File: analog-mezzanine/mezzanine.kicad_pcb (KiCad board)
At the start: 2 copper layers, 90 x 90 mm, 133 parts, among them J7 LD15P24A4GV00LF, U1 minus TPS7A3001MDGNTEP, U10 minus TPS7A3001MDGNTEP, U11 plus TPS7A4901DGNT, U12 BUF602xDBV, U2 plus TPS7A4901DGNT, U3 BUF602xDBV, U4 minus TPS7A3001MDGNTEP, U5 plus TPS7A4901DGNT, U6 BUF602xDBV, U7 minus TPS7A3001MDGNTEP, U8 plus TPS7A4901DGNT, U9 BUF602xDBV

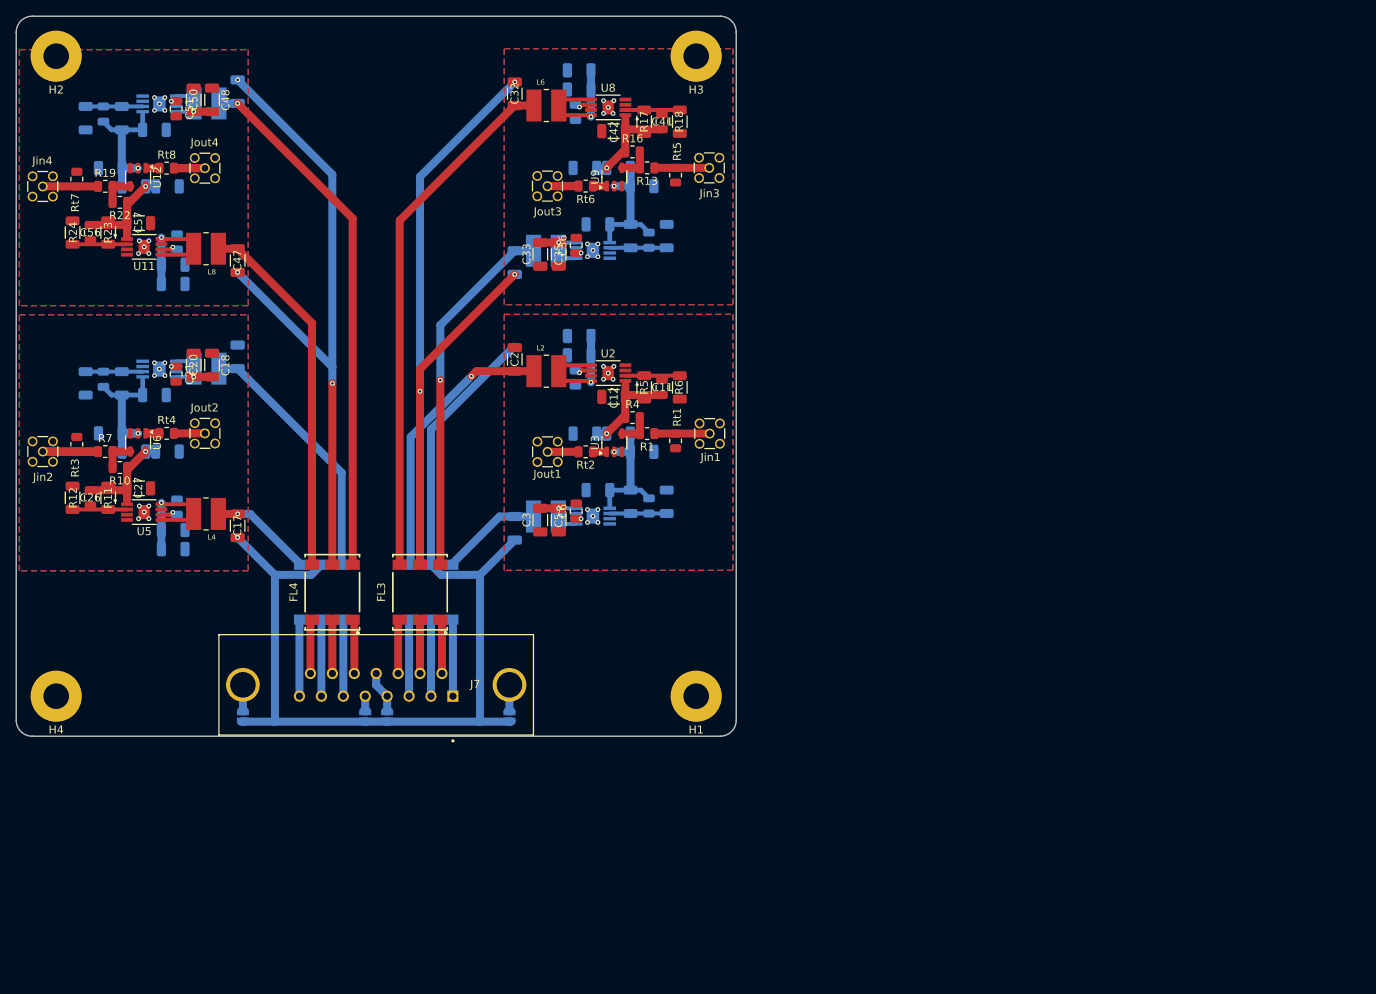
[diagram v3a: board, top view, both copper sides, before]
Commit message: update layout: central D connector
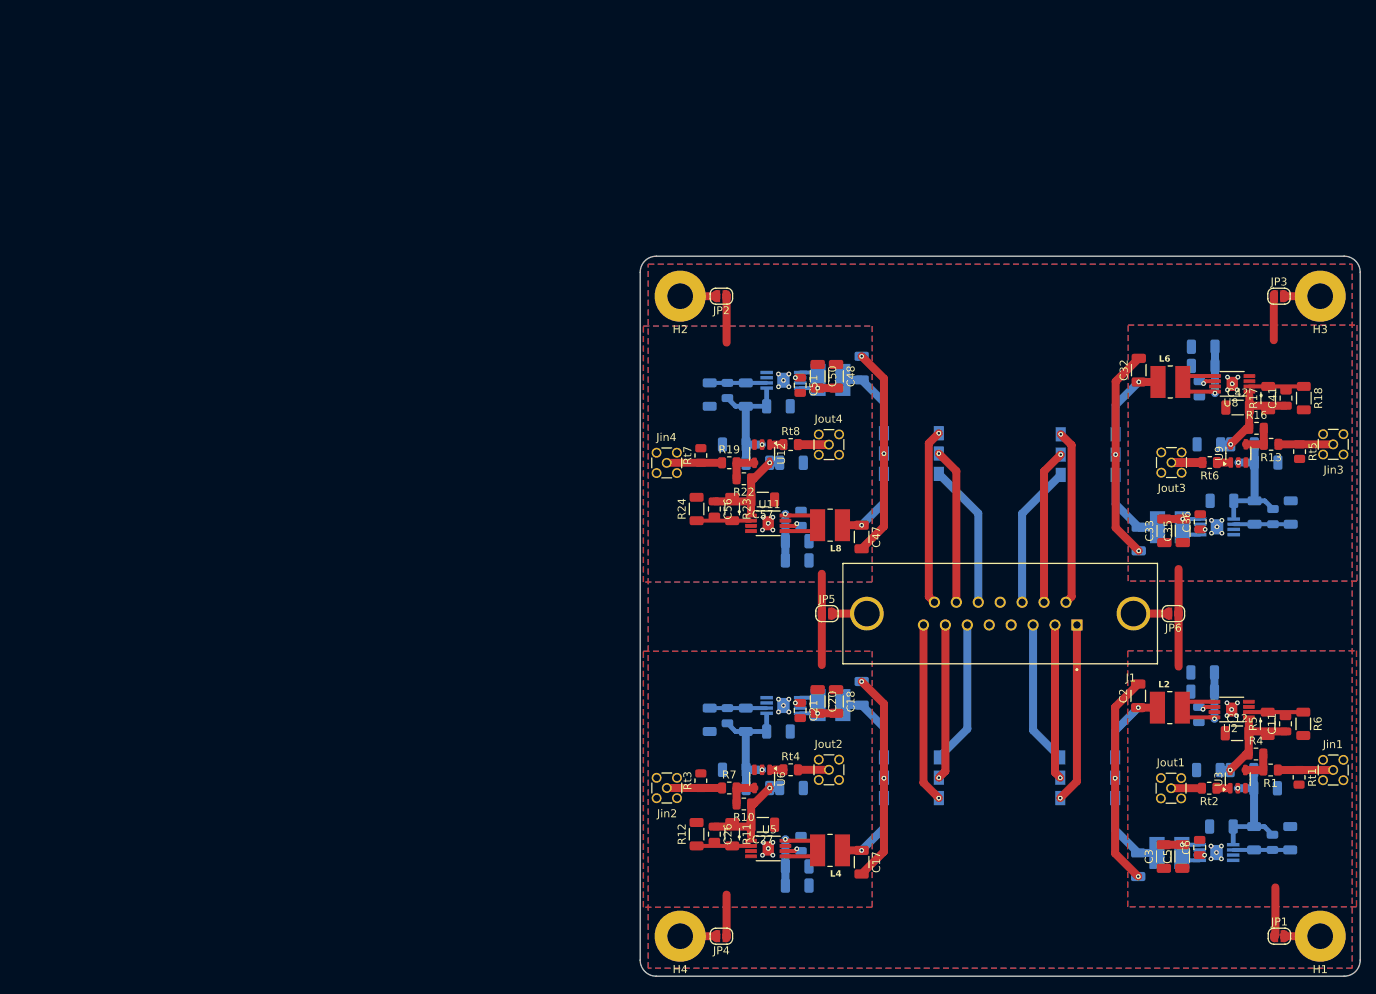
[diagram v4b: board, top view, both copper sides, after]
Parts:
- added JP1: jmp, Jumper:SolderJumper-2_P1.3mm_Open_RoundedPad1.0x1.5mm, F.Cu at (180.9, 135.0)
- added JP2: jmp, Jumper:SolderJumper-2_P1.3mm_Open_RoundedPad1.0x1.5mm, F.Cu at (111.2, 55.0)
- FL3, FL4: moved to B.Cu
- JP3, JP4: value SolderJumper_2_Open -> jmp; moved to F.Cu
- JP5: renamed from JP1; moved to F.Cu
- JP6: renamed from JP2; moved to F.Cu
- moved JP3 125.7 mm to (180.8, 55.0), turned to 0 degrees
- moved C27 88.6 mm to (116.3, 121.1)
- moved C16 88.6 mm to (128.7, 104.6)
- moved C17 88.6 mm to (128.7, 125.7)
- moved C18 88.6 mm to (125.5, 105.7)
- moved C19 88.6 mm to (120.6, 128.7)
- moved C20 88.6 mm to (123.2, 105.7)
- moved C21 88.6 mm to (121.0, 106.8)
- moved C22 88.6 mm to (121.1, 123.4)
- moved C23 88.6 mm to (120.6, 126.3)
- moved C24 88.6 mm to (118.3, 109.4)
- moved C25 88.6 mm to (111.9, 107.4)
- moved C26 88.6 mm to (110.3, 122.2)
- moved C28 88.6 mm to (112.8, 114.2)
- moved C29 88.6 mm to (119.9, 116.5)
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- renumbered J7 to J1
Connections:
- FL3 pad 4: /+7C -> /-7C
- FL3 pad 6: /-7C -> /+7C
- FL4 pad 4: /+7D -> /-7D
- FL4 pad 6: /-7D -> /+7D
- H1 pad 1: unconnected-(H1-Pad1) -> /infill-pour
- H2 pad 1: unconnected-(H2-Pad1) -> /infill-pour
- H3 pad 1: unconnected-(H3-Pad1) -> /infill-pour
- H4 pad 1: unconnected-(H4-Pad1) -> /infill-pour
- J1 pad 12: Net-(JP4-B) -> unconnected-(J1-Pad12)
- J1 pad 4: Net-(JP4-B) -> unconnected-(J1-Pad4)
- J1 pad 5: Net-(JP3-B) -> unconnected-(J1-Pad5)
- JP3 pad 2: Net-(JP3-B) -> /infill-pour
- JP4 pad 2: Net-(JP4-B) -> /infill-pour
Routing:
- net GND: track 294.4 -> 152.0 mm, vias 47 -> 48
- net /-7D: track 66.0 -> 10.2 mm, vias 1 -> 0
- net /+7C: track 65.8 -> 10.1 mm, vias 0 -> 1
- net /+7D: track 45.8 -> 9.97 mm, vias 0 -> 1
- net /-7C: track 45.4 -> 10.1 mm, vias 1 -> 0
- net /+7A: track 34.8 -> 9.82 mm
- net /-7B: track 32.2 -> 10.0 mm
- net /infill-pour: track 0.00 -> 17.9 mm
- net Net-(FL4-1): track 6.81 -> 21.9 mm, vias 0 -> 1
- net Net-(FL3-5): track 6.81 -> 21.8 mm, vias 0 -> 1
- net Net-(FL1-1): track 9.65 -> 22.5 mm, vias 0 -> 1
- net Net-(FL2-5): track 9.65 -> 22.4 mm, vias 0 -> 1
- net Net-(FL4-3): track 6.73 -> 19.5 mm, vias 0 -> 1
- net Net-(FL3-3): track 6.73 -> 19.3 mm, vias 0 -> 1
- net Net-(FL4-5): track 6.81 -> 18.1 mm
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- added copper zone on B.Cu, net /infill-pour
- added copper zone on F.Cu, net /infill-pour
